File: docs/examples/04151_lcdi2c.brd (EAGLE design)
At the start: 70.6 x 33.5 mm, 14 parts, among them IC1 PCF8574T, IC2 78L05Z

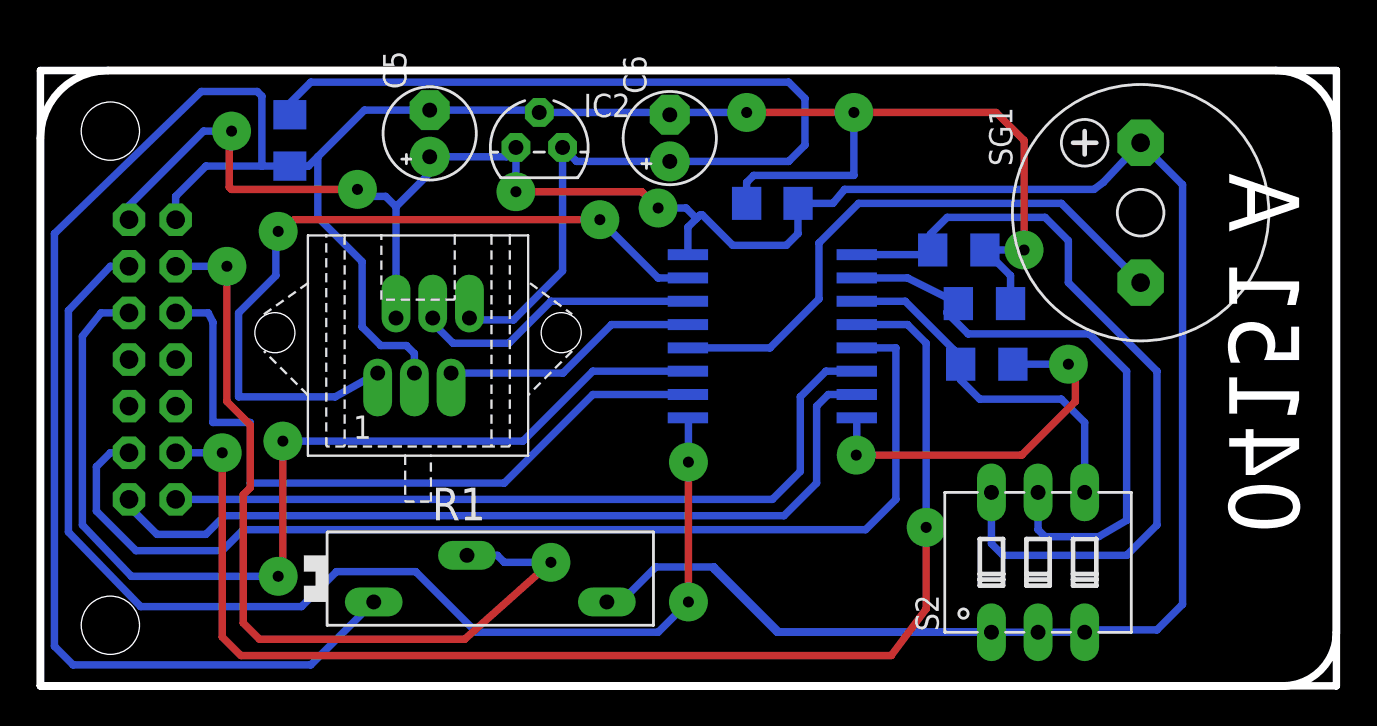
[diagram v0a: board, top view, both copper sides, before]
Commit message: Updated docs re: javaw.exe on Windows. Added pour to top of 04151_lcdi2c.brd file. Exploded components and moved text off edge to prevent isolation rectangle from extending past board edges.
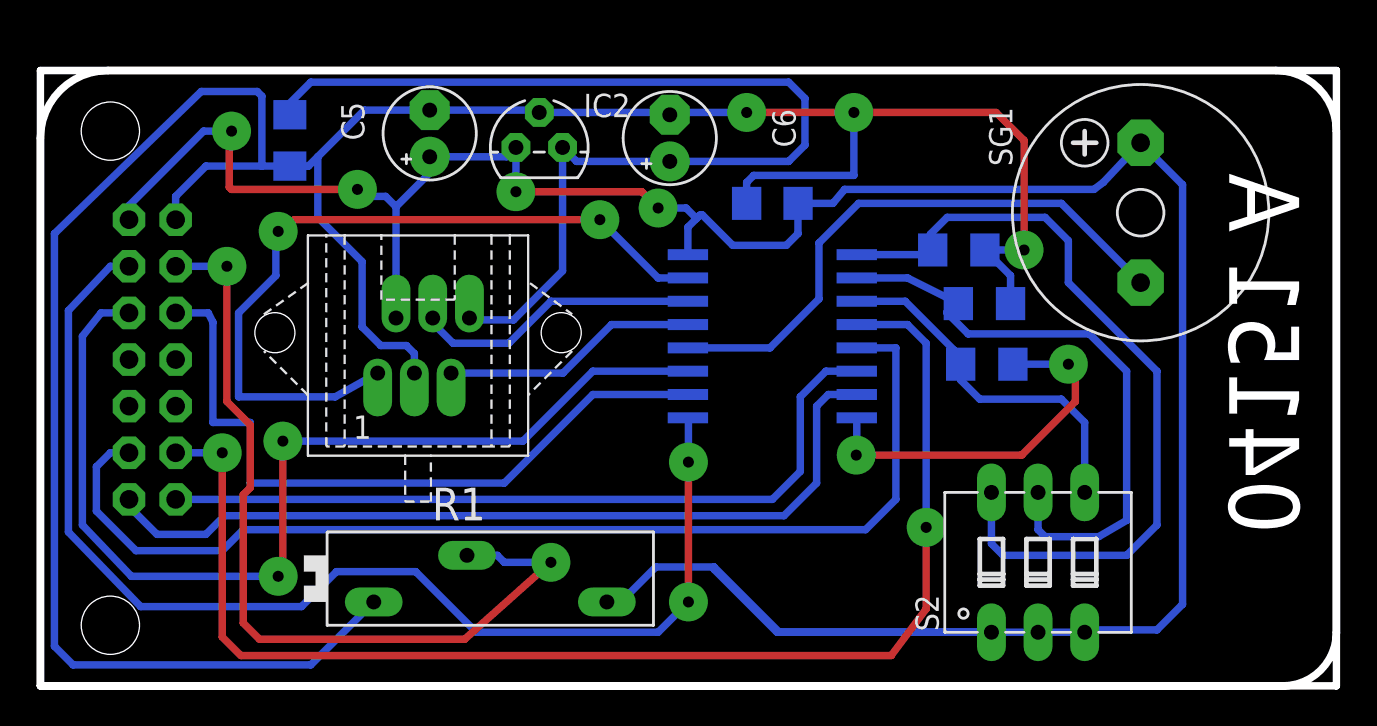
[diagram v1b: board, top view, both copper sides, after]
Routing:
- added copper zone on layer 1, net GND
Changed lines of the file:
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@@
 <element name="C4" library="rcl" package="C1206" value="100nf" x="13.589" y="29.718" rot="MR270"/>
 <element name="IC2" library="linear" package="TO92" value="78L05Z" x="27.178" y="29.337"/>
-<element name="C5" library="rcl" package="!FAT_E2,5-5" value="" x="21.209" y="30.099" rot="R90"/>
-<element name="C6" library="rcl" package="!FAT_E2,5-5" value="" x="34.29" y="29.845" rot="R90"/>
+<element name="C5" library="rcl" package="!FAT_E2,5-5" value="" x="21.209" y="30.099" smashed="yes" rot="R90">
+<attribute name="NAME" x="17.653" y="29.718" size="1.27" layer="25" ratio="10" rot="R90"/>
+<attribute name="VALUE" x="23.622" y="32.512" size="1.27" layer="27" ratio="10" rot="R90"/>
+</element>
+<element name="C6" library="rcl" package="!FAT_E2,5-5" value="" x="34.29" y="29.845" smashed="yes" rot="R90">
+<attribute name="NAME" x="41.148" y="29.337" size="1.27" layer="25" ratio="10" rot="R90"/>
+<attribute name="VALUE" x="36.703" y="32.258" size="1.27" layer="27" ratio="10" rot="R90"/>
+</element>
 </elements>
 <signals>
@@
 <wire x1="1.778" y1="1.143" x2="14.732" y2="1.143" width="0.4064" layer="16"/>
 <wire x1="14.732" y1="1.143" x2="18.161" y2="4.572" width="0.4064" layer="16"/>
-<wire x1="52.857" y1="20.828" x2="52.984" y2="17.526" width="0" layer="19" extent="16-16"/>
+<polygon width="0.3048" layer="1" isolate="0.5334" orphans="yes" rank="6">
+<vertex x="0" y="0"/>
+<vertex x="70.612" y="0"/>
+<vertex x="70.612" y="33.528"/>
+<vertex x="0" y="33.528"/>
+</polygon>
 </signal>
 <signal name="VCC">
